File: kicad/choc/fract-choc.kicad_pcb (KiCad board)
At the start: 2 copper layers, 180 x 68 mm, 91 parts, among them J1 Conn_01x02, SW1 SW_Push, SW10 SW_Push, SW11 SW_Push, SW12 SW_Push, SW13 SW_Push, SW14 SW_Push, SW15 SW_Push, SW16 SW_Push, SW17 SW_Push, SW18 SW_Push, SW19 SW_Push, SW2 SW_Push, SW20 SW_Push, SW21 SW_Push, SW22 SW_Push, SW23 SW_Push, SW24 SW_Push, SW25 SW_Push, SW26 SW_Push, SW27 SW_Push, SW28 SW_Push, SW29 SW_Push, SW3 SW_Push, SW30 SW_Push, SW31 SW_Push, SW32 SW_Push, SW33 SW_Push, SW34 SW_Push, SW35 SW_Push, SW36 SW_Push, SW37 SW_Push, SW38 SW_Push, SW39 SW_Push, SW4 SW_Push, SW40 SW_Push, SW5 SW_Push, SW6 SW_Push, SW7 SW_Push, SW8 SW_Push, SW9 SW_Push, U1 nice!nano

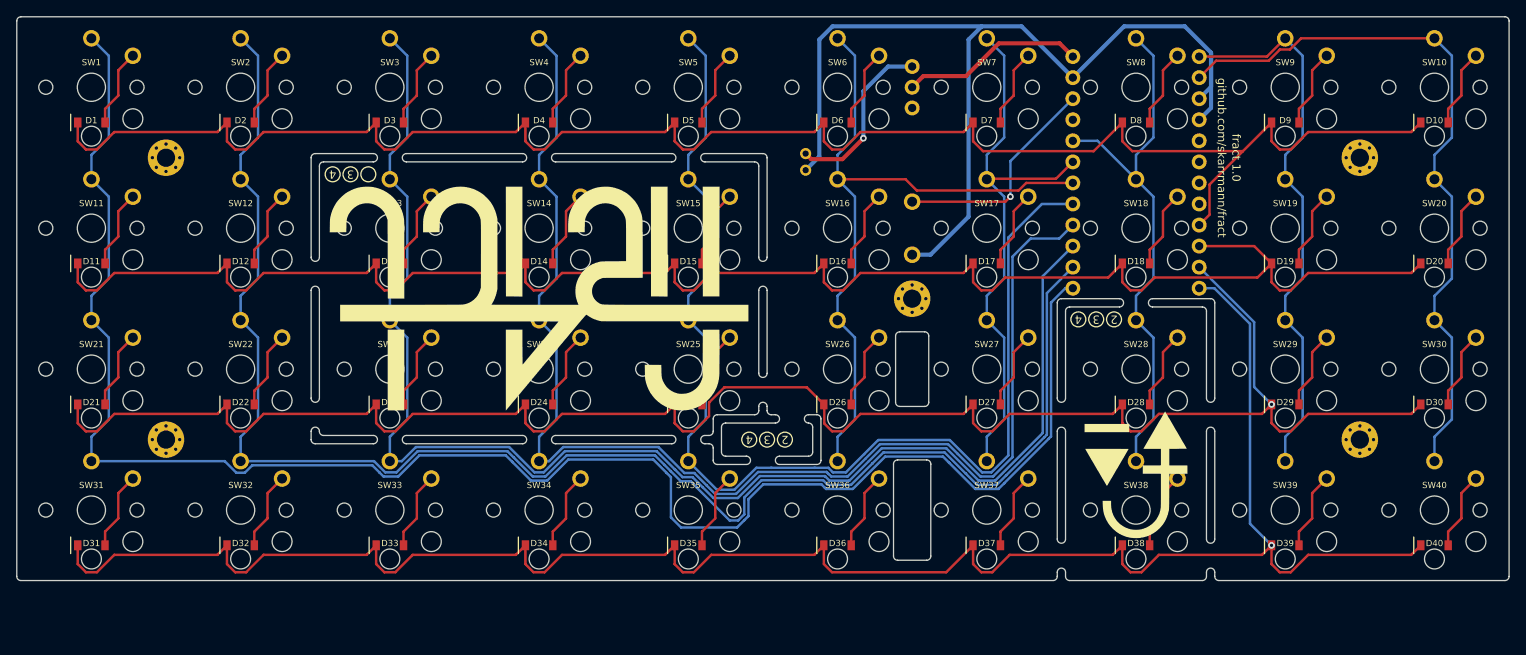
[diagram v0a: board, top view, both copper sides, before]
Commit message: Convert to 34 keys with top plates
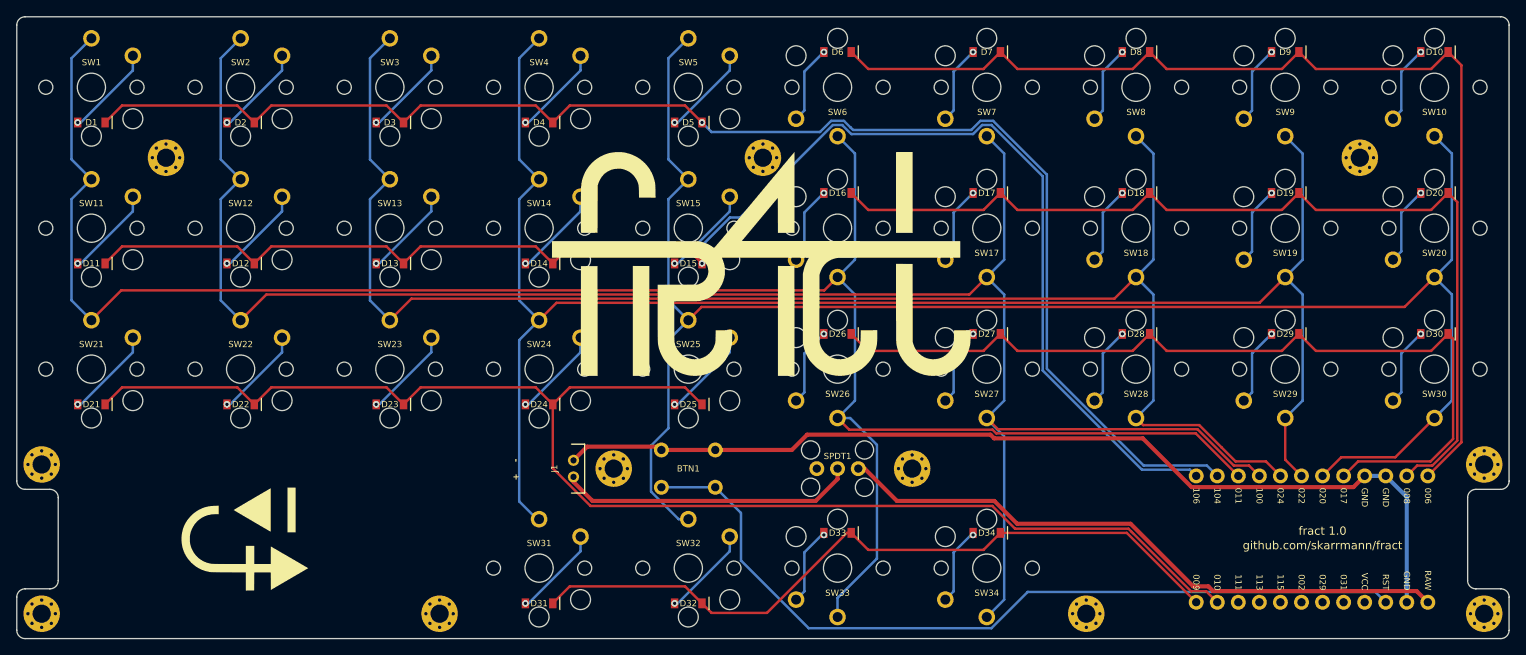
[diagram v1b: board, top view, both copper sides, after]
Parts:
- removed D35, D36, D37, D38, D39, D40: D, fract-footprints:D_SOD-123
- removed SW35, SW36, SW37, SW38, SW39, SW40: SW_Push, fract-footprints:SW_Choc
- added CUTOUT1: Cutout-nice!nano, fract-footprints:Cutout_nice!nano, F.Cu at (21.0, 86.5)
- added CUTOUT2: Cutout-SW_SPDT, fract-footprints:Cutout_SW_EG1218, F.Cu at (96.0, 78.0)
- added CUTOUT3: Cutout-BTN, fract-footprints:Cutout_SW_Push_6mm, F.Cu at (114.0, 78.0)
- added CUTOUT4: Cutout-Conn, fract-footprints:Cutout_JST_PH_S2B-PH-K_1x02_P2.00mm_Horizontal, F.Cu at (126.5, 78.0)
- added H10: Hole_Pad, fract-footprints:Mount_M2, F.Cu at (192.0, 95.5)
- added H2: Hole_Pad, fract-footprints:Mount_M2, F.Cu at (105.0, 40.5)
- added H6: Hole_Pad, fract-footprints:Mount_M2, F.Cu at (192.0, 77.5)
- added H7: Hole_Pad, fract-footprints:Mount_M2, F.Cu at (18.0, 95.5)
- added H8: Hole_Pad, fract-footprints:Mount_M2, F.Cu at (66.0, 95.5)
- added H9: Hole_Pad, fract-footprints:Mount_M2, F.Cu at (144.0, 95.5)
- added LOGO3: Logo-Name, fract-footprints:Logo_Fract_Name, F.Cu at (104.8, 53.3)
- BTN1: footprint fract-footprints:SW_PTS636 -> fract-footprints:SW_Push_6mm; moved to F.Cu
- J1, SPDT1, U1: moved to F.Cu
- LOGO2: value Logo-Name -> Logo; footprint fract-footprints:Logo_Fract_Name -> fract-footprints:Logo_Fract; moved to B.Cu
- moved LOGO1 107.8 mm to (42.5, 86.5), turned to 90 degrees
- moved H4 90.1 mm to (87.0, 78.0)
- moved U1 73.2 mm to (189.0, 86.5), turned to -90 degrees
- moved D31 54.5 mm to (78.0, 94.2), turned to 180 degrees
- moved D32 54.5 mm to (96.0, 94.2), turned to 180 degrees
- moved SW31 54.5 mm to (78.0, 90.0)
- moved SW32 54.5 mm to (96.0, 90.0)
- moved SW33 54.5 mm to (114.0, 90.0), turned to 180 degrees
- moved SW34 54.5 mm to (132.0, 90.0), turned to 180 degrees
- moved D33 54.0 mm to (114.0, 85.8), turned to 180 degrees
- moved D34 54.0 mm to (132.0, 85.8), turned to 180 degrees
- moved SPDT1 46.9 mm to (114.0, 78.0)
- moved J1 46.6 mm to (83.5, 78.0), turned to -90 degrees
- moved LOGO2 45.8 mm to (42.5, 86.5), turned to -90 degrees
- moved BTN1 39.6 mm to (96.0, 78.0)
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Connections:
- D10 pad 1: ROW1 -> ROW2
- D11 pad 1: ROW2 -> ROW3
- D12 pad 1: ROW2 -> ROW3
- D13 pad 1: ROW2 -> ROW3
- D14 pad 1: ROW2 -> ROW3
- D15 pad 1: ROW2 -> ROW3
- D16 pad 1: ROW2 -> ROW4
- D17 pad 1: ROW2 -> ROW4
- D18 pad 1: ROW2 -> ROW4
- D19 pad 1: ROW2 -> ROW4
- D20 pad 1: ROW2 -> ROW4
- D21 pad 1: ROW3 -> ROW5
- D22 pad 1: ROW3 -> ROW5
- D23 pad 1: ROW3 -> ROW5
- D24 pad 1: ROW3 -> ROW5
- D25 pad 1: ROW3 -> ROW5
- D26 pad 1: ROW3 -> ROW6
- D27 pad 1: ROW3 -> ROW6
- D28 pad 1: ROW3 -> ROW6
- D29 pad 1: ROW3 -> ROW6
- D30 pad 1: ROW3 -> ROW6
- D31 pad 1: ROW4 -> ROW7
- D32 pad 1: ROW4 -> ROW7
- D33 pad 1: ROW4 -> ROW7
- D34 pad 1: ROW4 -> ROW7
- D6 pad 1: ROW1 -> ROW2
- D7 pad 1: ROW1 -> ROW2
- D8 pad 1: ROW1 -> ROW2
- D9 pad 1: ROW1 -> ROW2
- SPDT1 pad 1: BAT+ -> RAW
- SPDT1 pad 2: RAW -> BAT+
- SW10 pad 1: COL10 -> COL5
- SW16 pad 1: COL6 -> COL1
- SW17 pad 1: COL7 -> COL2
- SW18 pad 1: COL8 -> COL3
- SW19 pad 1: COL9 -> COL4
- SW20 pad 1: COL10 -> COL5
- SW26 pad 1: COL6 -> COL1
- SW27 pad 1: COL7 -> COL2
- SW28 pad 1: COL8 -> COL3
- SW29 pad 1: COL9 -> COL4
- SW30 pad 1: COL10 -> COL5
- SW31 pad 1: COL1 -> COL4
- SW32 pad 1: COL2 -> COL5
- SW33 pad 1: COL3 -> COL1
- SW34 pad 1: COL4 -> COL2
- SW6 pad 1: COL6 -> COL1
- SW7 pad 1: COL7 -> COL2
- SW8 pad 1: COL8 -> COL3
- SW9 pad 1: COL9 -> COL4
- U1 pad 1: COL9 -> ROW2
- U1 pad 10: ROW2 -> COL1
- U1 pad 11: ROW3 -> ROW1
- U1 pad 12: ROW4 -> ROW3
- U1 pad 13: COL1 -> ROW7
- U1 pad 14: COL2 -> ROW5
- U1 pad 15: COL3 -> unconnected-(U1-111-Pad15)
- U1 pad 16: COL4 -> unconnected-(U1-113-Pad16)
- U1 pad 17: COL5 -> unconnected-(U1-115-Pad17)
- U1 pad 18: COL6 -> unconnected-(U1-002-Pad18)
- U1 pad 19: COL7 -> unconnected-(U1-029-Pad19)
- U1 pad 2: COL10 -> ROW4
- U1 pad 20: COL8 -> unconnected-(U1-031-Pad20)
- U1 pad 5: unconnected-(U1-017-Pad5) -> ROW6
- U1 pad 6: unconnected-(U1-020-Pad6) -> COL5
- U1 pad 7: unconnected-(U1-022-Pad7) -> COL4
- U1 pad 8: unconnected-(U1-024-Pad8) -> COL3
- U1 pad 9: ROW1 -> COL2
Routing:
- net ROW5: track 0.00 -> 173.3 mm
- net ROW4: track 233.9 -> 117.0 mm, vias 1 -> 0
- net ROW6: track 0.00 -> 106.8 mm
- net ROW7: track 0.00 -> 88.9 mm
- net COL10: track 86.6 -> 0.00 mm
- net COL6: track 85.5 -> 0.00 mm
- net ROW2: track 207.8 -> 132.3 mm
- net COL5: track 137.4 -> 212.4 mm
- net RESET: track 27.0 -> 100.1 mm, vias 1 -> 0
- net COL9: track 67.5 -> 0.00 mm
- net COL7: track 67.5 -> 0.00 mm
- net COL8: track 65.8 -> 0.00 mm
- net RAW: track 22.2 -> 75.4 mm
- net COL4: track 154.9 -> 201.6 mm
- net ROW3: track 221.0 -> 178.8 mm
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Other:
- board size 180 x 68 mm -> 180 x 75 mm
- board text removed: "2"
- board text removed: "3"
- board text removed: "4"
- board text removed: "JLCJLCJLCJLC"

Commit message: Clean up design files
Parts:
- moved CUTOUT4 6.90 mm to (133.4, 78.0)
- moved J1 6.90 mm to (76.6, 78.0)
- moved LOGO3 6.70 mm to (105.0, 60.0)
- renumbered H9 to H10, H10 to H11, H2 to H3, H3 to H4, H4 to H5, H5 to H6, H6 to H7, H7 to H8, H8 to H9
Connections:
- H2 pad 1: unconnected-(H2-Pad1)_2 -> unconnected-(H2-Pad1)_8
- H3 pad 1: unconnected-(H2-Pad1)_2 -> unconnected-(H3-Pad1)_2
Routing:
- net ROW5: track 173.3 -> 186.8 mm
- net GND: track 119.1 -> 126.0 mm
- net BAT+: track 35.8 -> 42.3 mm
- net COL4: track 201.6 -> 202.5 mm

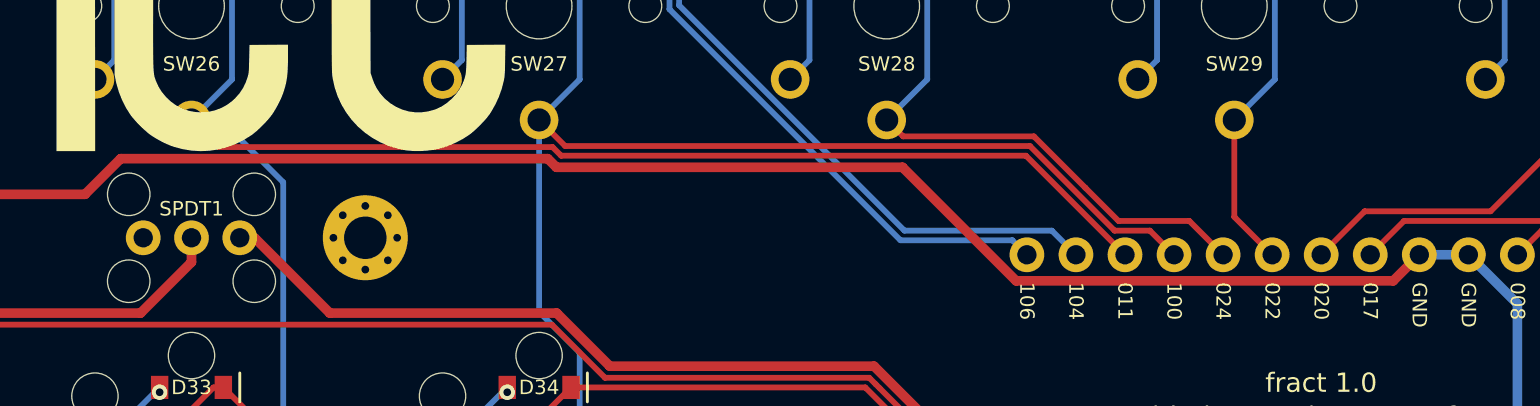
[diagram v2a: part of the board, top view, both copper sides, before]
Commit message: Change on/off switch part
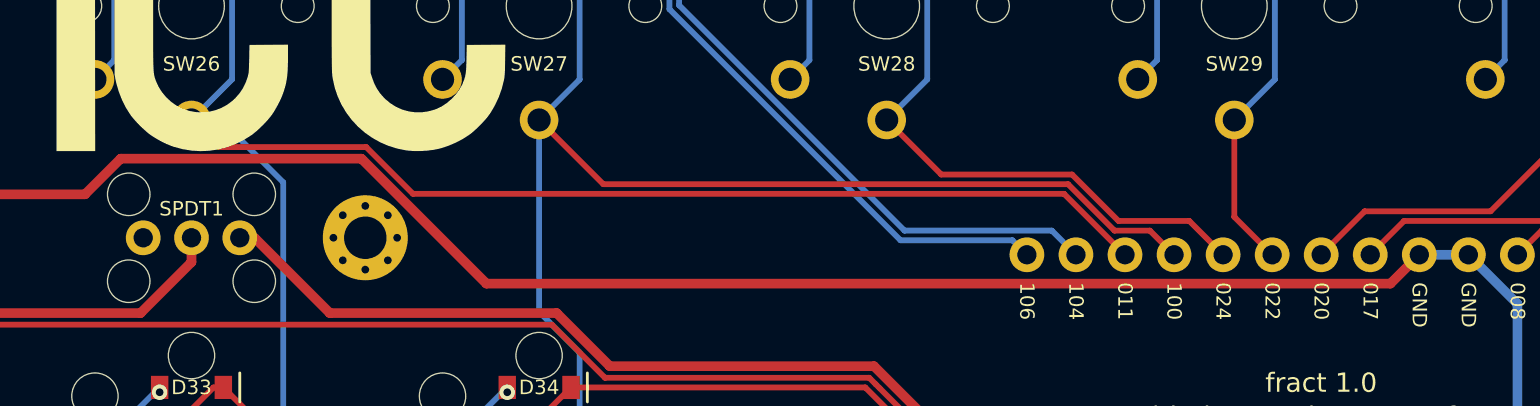
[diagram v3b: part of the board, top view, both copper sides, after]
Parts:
- CUTOUT2: footprint fract-footprints:Cutout_SW_EG1218 -> fract-footprints:Cutout_SW_SS12D00
- SPDT1: footprint fract-footprints:SW_EG1218 -> fract-footprints:SW_SS12D00
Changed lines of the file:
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@@
 		)
 	)
-	(footprint "fract-footprints:SW_EG1218"
+	(footprint "fract-footprints:SW_SS12D00"
 		(layer "F.Cu")
 		(at 114 78 180)
-		(descr "Slide Switch, E-Switch EG1218")
+		(descr "Slide Switch, SS12D00")
 		(tags "slide switch, on-on")
 		(property "Reference" "SPDT1"
@@
 			)
 		)
-		(property "Footprint" "fract-footprints:SW_EG1218"
+		(property "Footprint" "fract-footprints:SW_SS12D00"
 			(at 0 0 180)
 			(layer "F.Fab")
@@
 		)
 	)
-	(footprint "fract-footprints:Cutout_SW_EG1218"
+	(footprint "fract-footprints:Cutout_SW_SS12D00"
 		(layer "F.Cu")
 		(at 96 78 180)
-		(descr "Cutout for Slide Switch, E-Switch EG1218")
+		(descr "Cutout for Slide Switch, SS12D00")
 		(tags "cutout, slide switch, on-on")
 		(property "Reference" "CUTOUT2"
@@
 			)
 		)
-		(property "Footprint" "fract-footprints:Cutout_SW_EG1218"
+		(property "Footprint" "fract-footprints:Cutout_SW_SS12D00"
 			(at 0 0 180)
 			(layer "F.Fab")
@@
 	)
 	(gr_arc
-		(start 98 76.75)
-		(mid 98.353553 76.896447)
-		(end 98.5 77.25)
+		(start 99.5 76.75)
+		(mid 99.853553 76.896447)
+		(end 100 77.25)
 		(stroke
 			(width 0.1)
@@
 	)
 	(gr_line
-		(start 98 79.25)
+		(start 99.5 79.25)
 		(end 97.75 79.25)
 		(stroke
@@
 	)
 	(gr_line
-		(start 98.5 78.75)
-		(end 98.5 77.25)
+		(start 100 78.75)
+		(end 100 77.25)
 		(stroke
 			(width 0.1)
@@
 	)
 	(gr_line
-		(start 94 79.25)
+		(start 92.5 79.25)
 		(end 94.25 79.25)
 		(stroke
@@
 	)
 	(gr_arc
-		(start 93.5 77.25)
-		(mid 93.646447 76.896447)
-		(end 94 76.75)
+		(start 92 77.25)
+		(mid 92.146447 76.896447)
+		(end 92.5 76.75)
 		(stroke
 			(width 0.1)
@@
 	)
 	(gr_line
-		(start 94 76.75)
+		(start 92.5 76.75)
 		(end 94.25 76.75)
 		(stroke
@@
 	)
 	(gr_line
-		(start 93.5 78.75)
-		(end 93.5 77.25)
+		(start 92 78.75)
+		(end 92 77.25)
 		(stroke
 			(width 0.1)
@@
 	)
 	(gr_arc
-		(start 94 79.25)
-		(mid 93.646447 79.103553)
-		(end 93.5 78.75)
+		(start 92.5 79.25)
+		(mid 92.146447 79.103553)
+		(end 92 78.75)
 		(stroke
 			(width 0.1)
@@
 	)
 	(gr_arc
-		(start 98.5 78.75)
-		(mid 98.353553 79.103553)
-		(end 98 79.25)
+		(start 100 78.75)
+		(mid 99.853553 79.103553)
+		(end 99.5 79.25)
 		(stroke
 			(width 0.1)
@@
 	)
 	(gr_line
-		(start 98 76.75)
+		(start 99.5 76.75)
 		(end 97.75 76.75)
 		(stroke
@@
 	)
 	(segment
-		(start 110.333705 73.903553)
-		(end 108.487258 75.75)
+		(start 177.58 78.88)
+		(end 176.085 80.375)
 		(width 0.5)
 		(layer "F.Cu")
@@
 	)
 	(segment
-		(start 92.75 75.75)
-		(end 99.25 75.75)
+		(start 129.271447 80.375)
+		(end 122.8 73.903553)
 		(width 0.5)
 		(layer "F.Cu")
@@
 	)
 	(segment
-		(start 132.447919 73.903553)
-		(end 110.333705 73.903553)
+		(start 110.333705 73.903553)
+		(end 108.487258 75.75)
 		(width 0.5)
 		(layer "F.Cu")
@@
 	)
 	(segment
-		(start 176.23 80.23)
-		(end 156.700811 80.23)
+		(start 92.75 75.75)
+		(end 99.25 75.75)
 		(width 0.5)
 		(layer "F.Cu")
@@
 	)
 	(segment
-		(start 92.75 75.75)
-		(end 92.35 75.35)
+		(start 176.085 80.375)
+		(end 129.271447 80.375)
 		(width 0.5)
 		(layer "F.Cu")
@@
 	)
 	(segment
-		(start 132.894366 74.35)
-		(end 132.447919 73.903553)
+		(start 92.75 75.75)
+		(end 92.35 75.35)
 		(width 0.5)
 		(layer "F.Cu")
@@
 	)
 	(segment
-		(start 156.700811 80.23)
-		(end 150.820811 74.35)
+		(start 122.8 73.903553)
+		(end 110.333705 73.903553)
 		(width 0.5)
 		(layer "F.Cu")
@@
 	)
 	(segment
-		(start 177.58 78.88)
-		(end 176.23 80.23)
-		(width 0.5)
-		(layer "F.Cu")
-		(net 1)
-	)
-	(segment
-		(start 150.820811 74.35)
-		(end 132.894366 74.35)
-		(width 0.5)
-		(layer "F.Cu")
-		(net 1)
-	)
-	(segment
 		(start 76.9 75.35)
 		(end 75.25 77)
@@
 	)
 	(segment
-		(start 162.34 78.88)
-		(end 157.21 73.75)
-		(width 0.3)
-		(layer "F.Cu")
-		(net 5)
-	)
-	(segment
 		(start 115.403553 73.303553)
 		(end 114 71.9)
@@
 	)
 	(segment
-		(start 133.142894 73.75)
-		(end 132.696447 73.303553)
+		(start 123.048528 73.303553)
+		(end 115.403553 73.303553)
 		(width 0.3)
 		(layer "F.Cu")
@@
 	)
 	(segment
-		(start 157.21 73.75)
-		(end 133.142894 73.75)
+		(start 162.34 78.88)
+		(end 159.185 75.725)
 		(width 0.3)
 		(layer "F.Cu")
@@
 	)
 	(segment
-		(start 132.696447 73.303553)
-		(end 115.403553 73.303553)
+		(start 125.469975 75.725)
+		(end 123.048528 73.303553)
+		(width 0.3)
+		(layer "F.Cu")
+		(net 5)
+	)
+	(segment
+		(start 159.185 75.725)
+		(end 125.469975 75.725)
 		(width 0.3)
 		(layer "F.Cu")
@@
 	)
 	(segment
-		(start 157.417106 73.25)
-		(end 133.35 73.25)
+		(start 159.392106 75.225)
+		(end 161.797106 77.63)
 		(width 0.3)
 		(layer "F.Cu")
@@
 	)
 	(segment
-		(start 163.63 77.63)
-		(end 161.797106 77.63)
+		(start 132 71.9)
+		(end 135.325 75.225)
 		(width 0.3)
 		(layer "F.Cu")
@@
 	)
 	(segment
-		(start 164.88 78.88)
-		(end 163.63 77.63)
+		(start 163.63 77.63)
+		(end 164.88 78.88)
 		(width 0.3)
 		(layer "F.Cu")
@@
 	)
 	(segment
-		(start 129.9 57)
-		(end 132 54.9)
+		(start 161.797106 77.63)
+		(end 163.63 77.63)
 		(width 0.3)
 		(layer "F.Cu")
@@
 	)
 	(segment
-		(start 161.797106 77.63)
-		(end 157.417106 73.25)
+		(start 129.9 57)
+		(end 132 54.9)
 		(width 0.3)
 		(layer "F.Cu")
@@
 	)
 	(segment
-		(start 42 60.1)
-		(end 45.1 57)
+		(start 135.325 75.225)
+		(end 159.392106 75.225)
 		(width 0.3)
 		(layer "F.Cu")
@@
 	)
 	(segment
-		(start 133.35 73.25)
-		(end 132 71.9)
+		(start 42 60.1)
+		(end 45.1 57)
 		(width 0.3)
 		(layer "F.Cu")
@@
 	)
 	(segment
-		(start 165.67 77.13)
+		(start 159.599212 74.725)
 		(end 162.004212 77.13)
 		(width 0.3)
@@
 	)
 	(segment
-		(start 167.42 78.88)
-		(end 165.67 77.13)
+		(start 152.825 74.725)
+		(end 159.599212 74.725)
 		(width 0.3)
 		(layer "F.Cu")
@@
 	)
 	(segment
-		(start 150.85 72.75)
-		(end 150 71.9)
+		(start 165.67 77.13)
+		(end 167.42 78.88)
 		(width 0.3)
 		(layer "F.Cu")
@@
 	)
 	(segment
-		(start 160.287106 75.412893)
-		(end 157.624213 72.75)
+		(start 147.4 57.5)
+		(end 150 54.9)
 		(width 0.3)
 		(layer "F.Cu")
@@
 	)
 	(segment
-		(start 162.004212 77.13)
-		(end 160.287106 75.412894)
-		(width 0.3)
-		(layer "F.Cu")
-		(net 8)
-	)
-	(segment
-		(start 147.4 57.5)
-		(end 150 54.9)
+		(start 150 71.9)
+		(end 152.825 74.725)
 		(width 0.3)
 		(layer "F.Cu")
@@
 	)
 	(segment
-		(start 157.624213 72.75)
-		(end 150.85 72.75)
-		(width 0.3)
-		(layer "F.Cu")
-		(net 8)
-	)
-	(segment
-		(start 160.287106 75.412894)
-		(end 160.287106 75.412893)
+		(start 162.004212 77.13)
+		(end 165.67 77.13)
 		(width 0.3)
 		(layer "F.Cu")
